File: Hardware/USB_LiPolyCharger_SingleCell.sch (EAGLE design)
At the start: 25 parts, among them J1 POWER_JACKPTH_LOCK, U1 MCP73831, X1 USBSMD

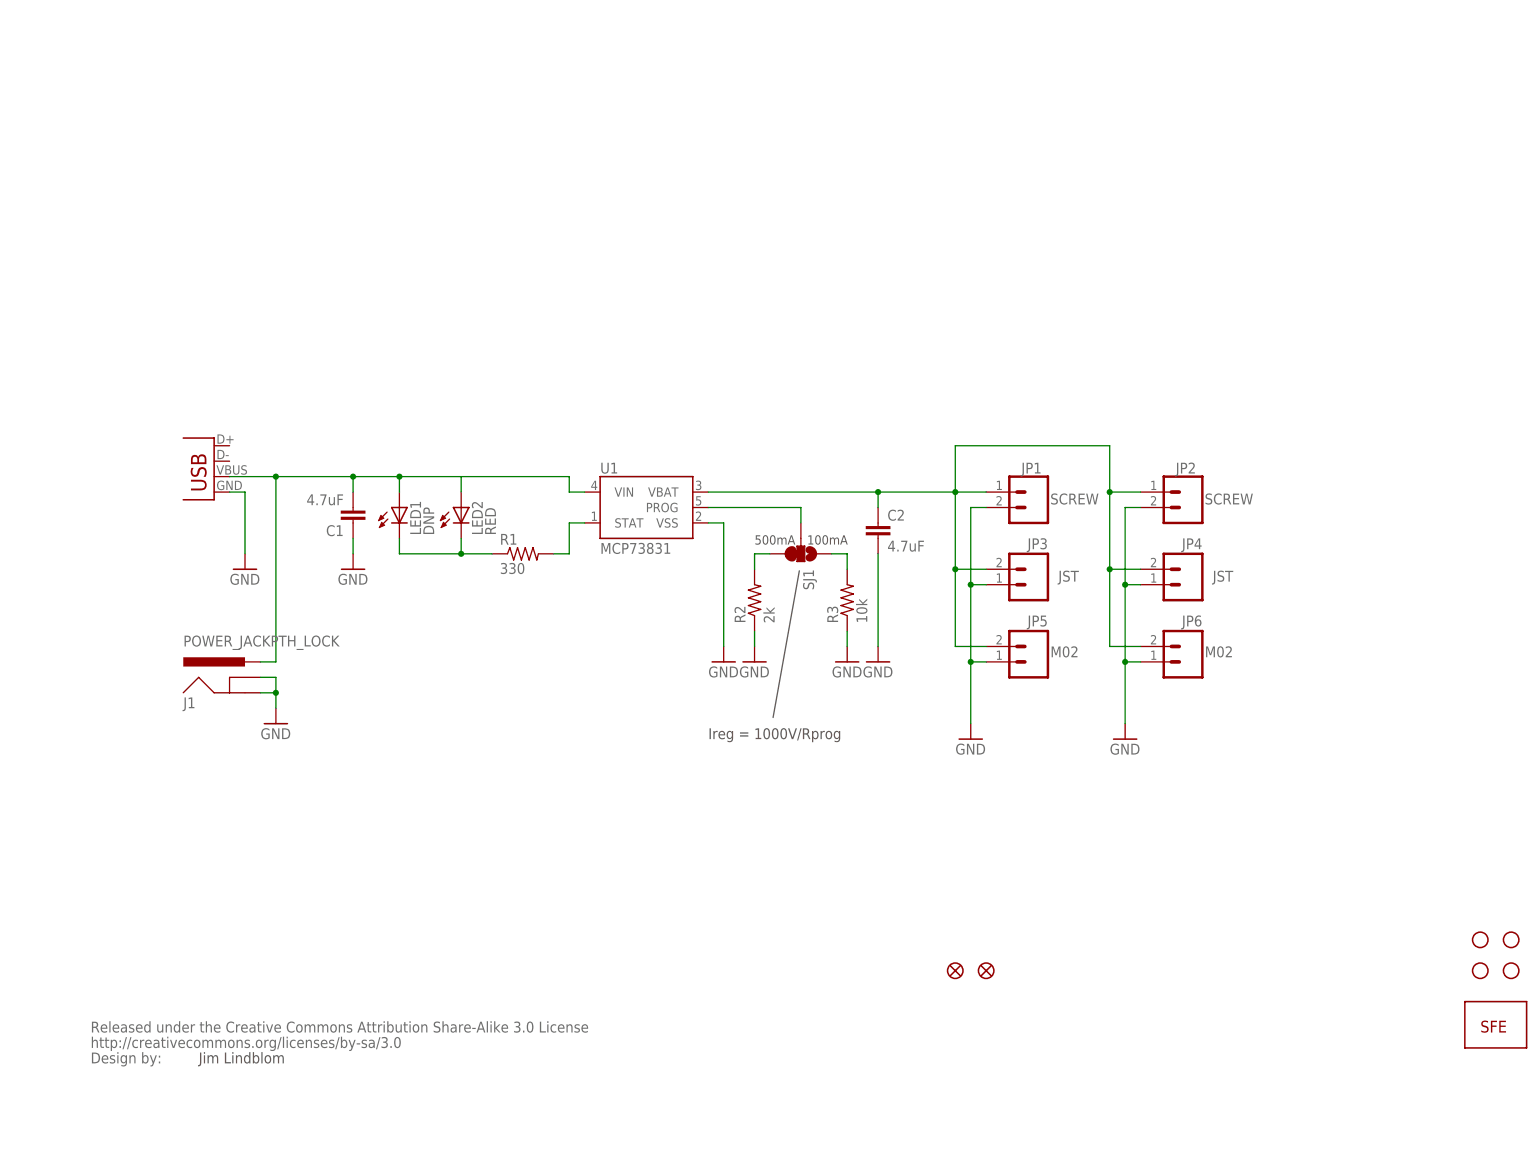
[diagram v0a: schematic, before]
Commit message: Added Diodes/Prog RES
Added 2x MBRA diodes to the power lines of the USB and Barrel jack .
Also added an optional PTH res for the PROG line.
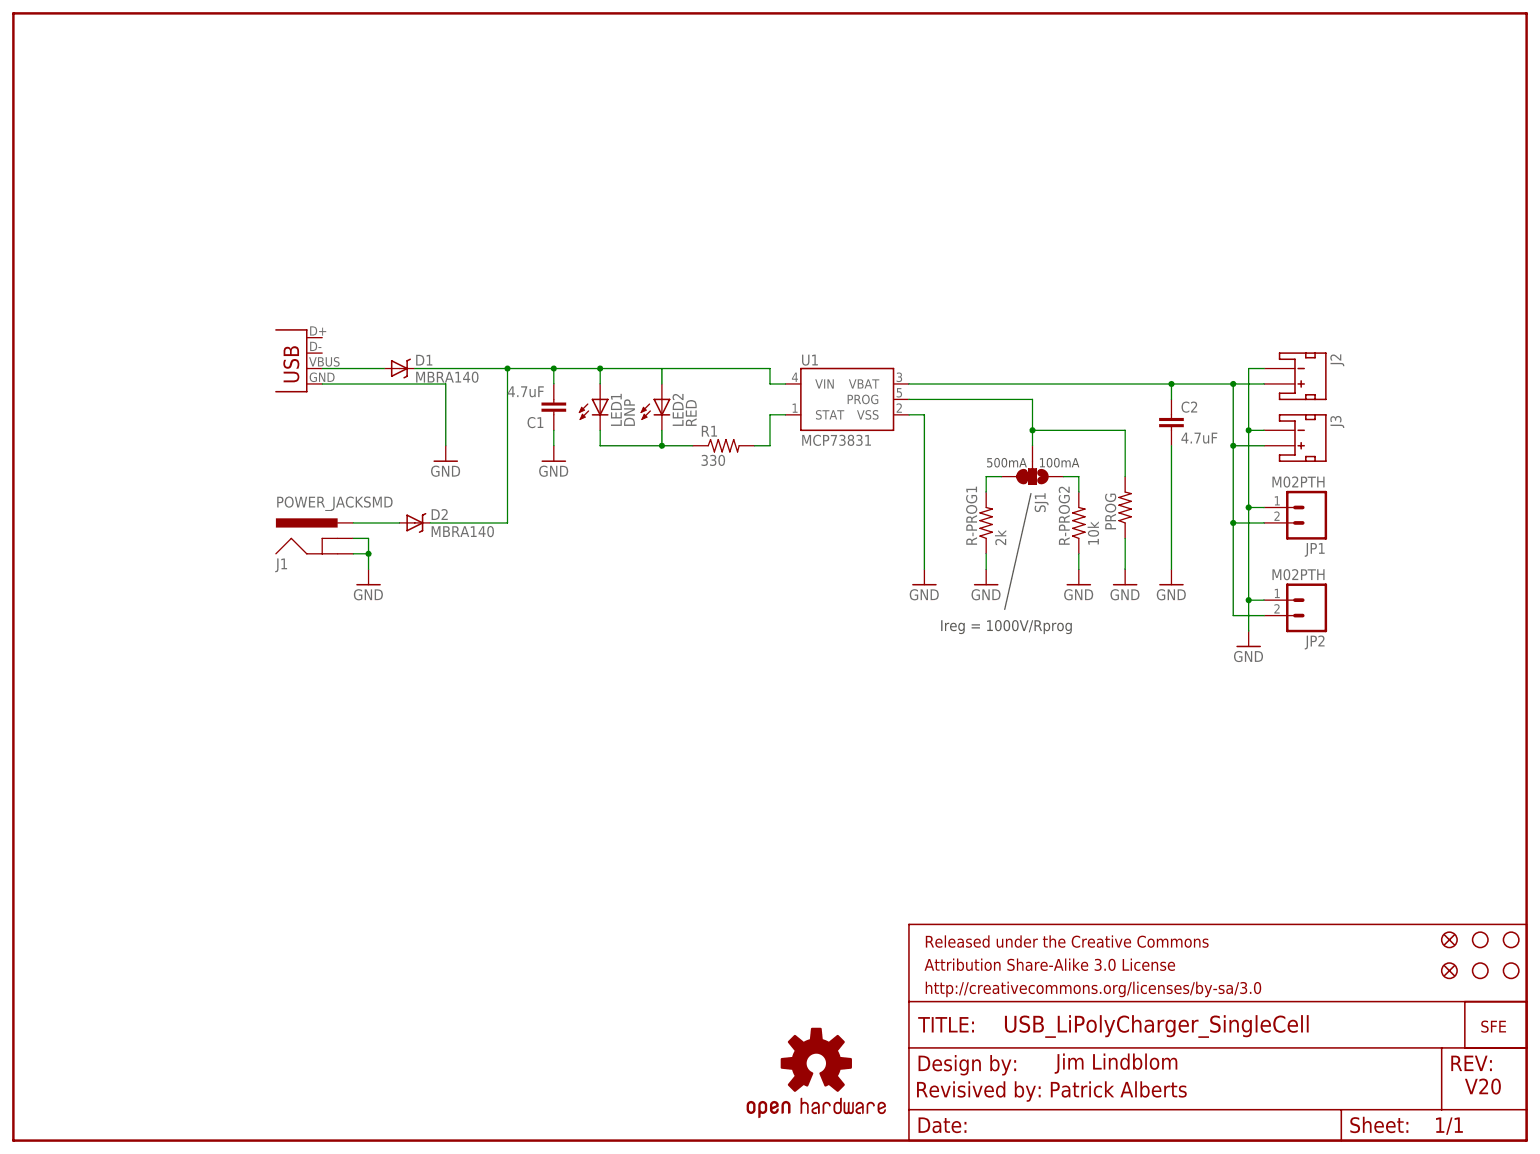
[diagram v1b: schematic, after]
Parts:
- removed JP3, JP4: JST, SparkFun:M02JST-PTH-2
- removed JP5, JP6: M02, SparkFun:M02PTH
- removed R2: 2k, SparkFun:RESISTOR0603-RES
- removed R3: 10k, SparkFun:RESISTOR0603-RES
- removed U$: CREATIVE_COMMONS, SparkFun:CREATIVE_COMMONS
- added D1, D2: MBRA140, SparkFun-DiscreteSemi:MBRA140
- added FRAME1: FRAME-LETTER, SparkFun-Aesthetics:FRAME-LETTER
- added J2, J3: (no value), SparkFun-Connectors:JST_2MM_MALE
- added LOGO1: OSHW-LOGOS, SparkFun-Aesthetics:OSHW-LOGOS
- added PROG: (no value), SparkFun-Resistors:RESISTORAXIAL-0.3
- added R-PROG1: 2k, SparkFun-Resistors:2.0KOHM1/10W5%(0603)
- added R-PROG2: 10k, SparkFun-Resistors:10KOHM1/10W1%(0603)0603
- C1, C2: device SparkFun:CAP0603-CAP -> SparkFun-Capacitors:4.7UF-6.3V-10%(0603)0603
- J1: value POWER_JACKPTH_LOCK -> POWER_JACKSMD; device SparkFun:POWER_JACKPTH_LOCK -> SparkFun-Connectors:POWER_JACKSMD
- JP1, JP2: value SCREW -> M02PTH; device SparkFun:M023.5MM-NO_SILK -> SparkFun-Connectors:M02PTH
- LED2: device SparkFun:LED0603 -> SparkFun-LED:LED-RED0603
- R1: device SparkFun:RESISTOR0603-RES -> SparkFun-Resistors:330OHM1/10W1%(0603)
- U1: device SparkFun:MCP73831 -> SparkFun-PowerIC:MCP73831
- X1: device SparkFun:USBSMD -> SparkFun-Connectors:USBSMD
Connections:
- removed net VBAT: C2.1, JP1.1, JP2.1, JP3.2, JP4.2, JP5.2, JP6.2, U1.VBAT
- new net N$10: C2.1, J2.+, J3.+, JP1.2, JP2.2, U1.VBAT
- new net N$6: D1.A, X1.VBUS
- new net N$8: D2.A, J1.PWR
- net GND: now also J2.-, J3.-, JP1.1, JP2.1, PROG.1, R-PROG1.1, R-PROG2.1; no longer JP1.2, JP2.2, JP3.1, JP4.1, JP5.1, JP6.1, R2.1, R3.1
- net N$1: now also D1.C, D2.C; no longer J1.PWR, X1.VBUS
- net N$4: now also R-PROG1.2; no longer R2.2
- net N$7: now also R-PROG2.2; no longer R3.2
- net PROG: now also PROG.2
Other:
- note added: "Revisived by: Patrick Alberts"
- note added: "V20"
- moved on the sheet: C1, C2, J1, JP1, JP2, LED1, LED2, R1, SJ1, U1
